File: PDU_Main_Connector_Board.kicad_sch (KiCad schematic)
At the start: 2 parts, among them J1 776228-1, J2 Conn_02x02_Odd_Even

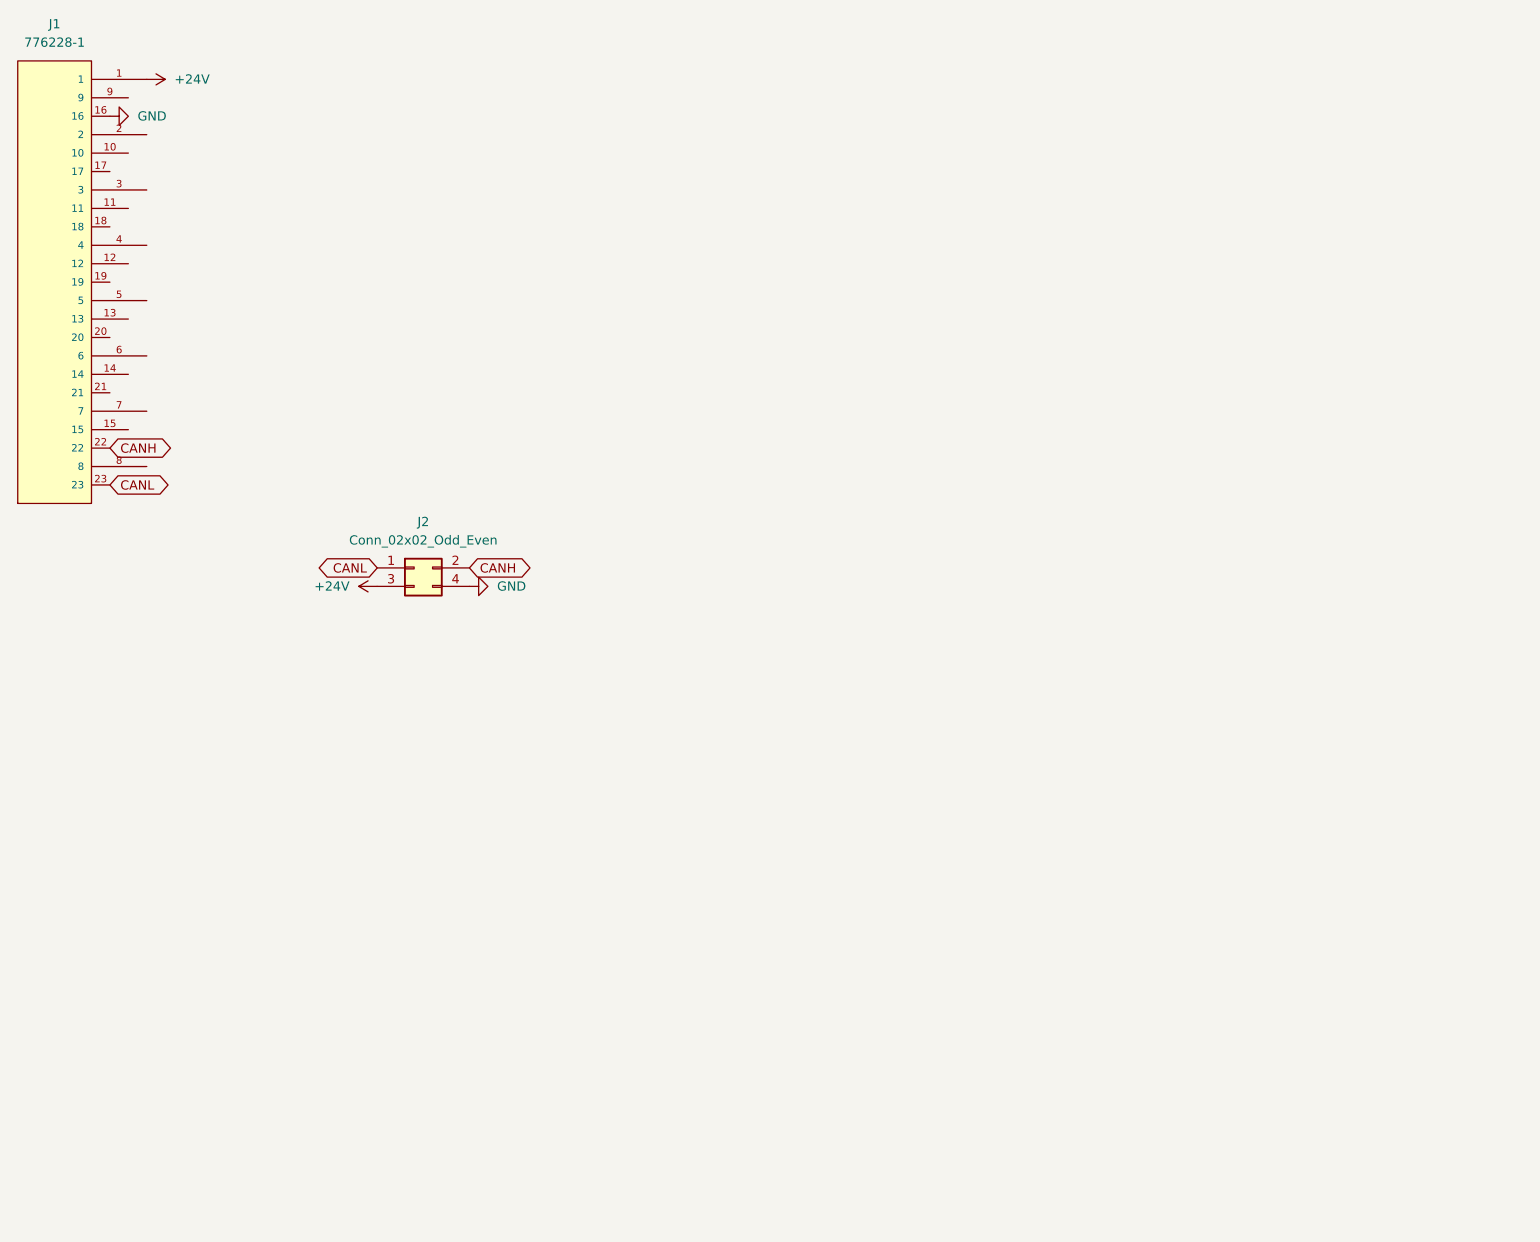
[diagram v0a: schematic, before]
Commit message: VER1.0: добавил схему по госту в доки, добавил дублирование CAN, добавил новые герберы
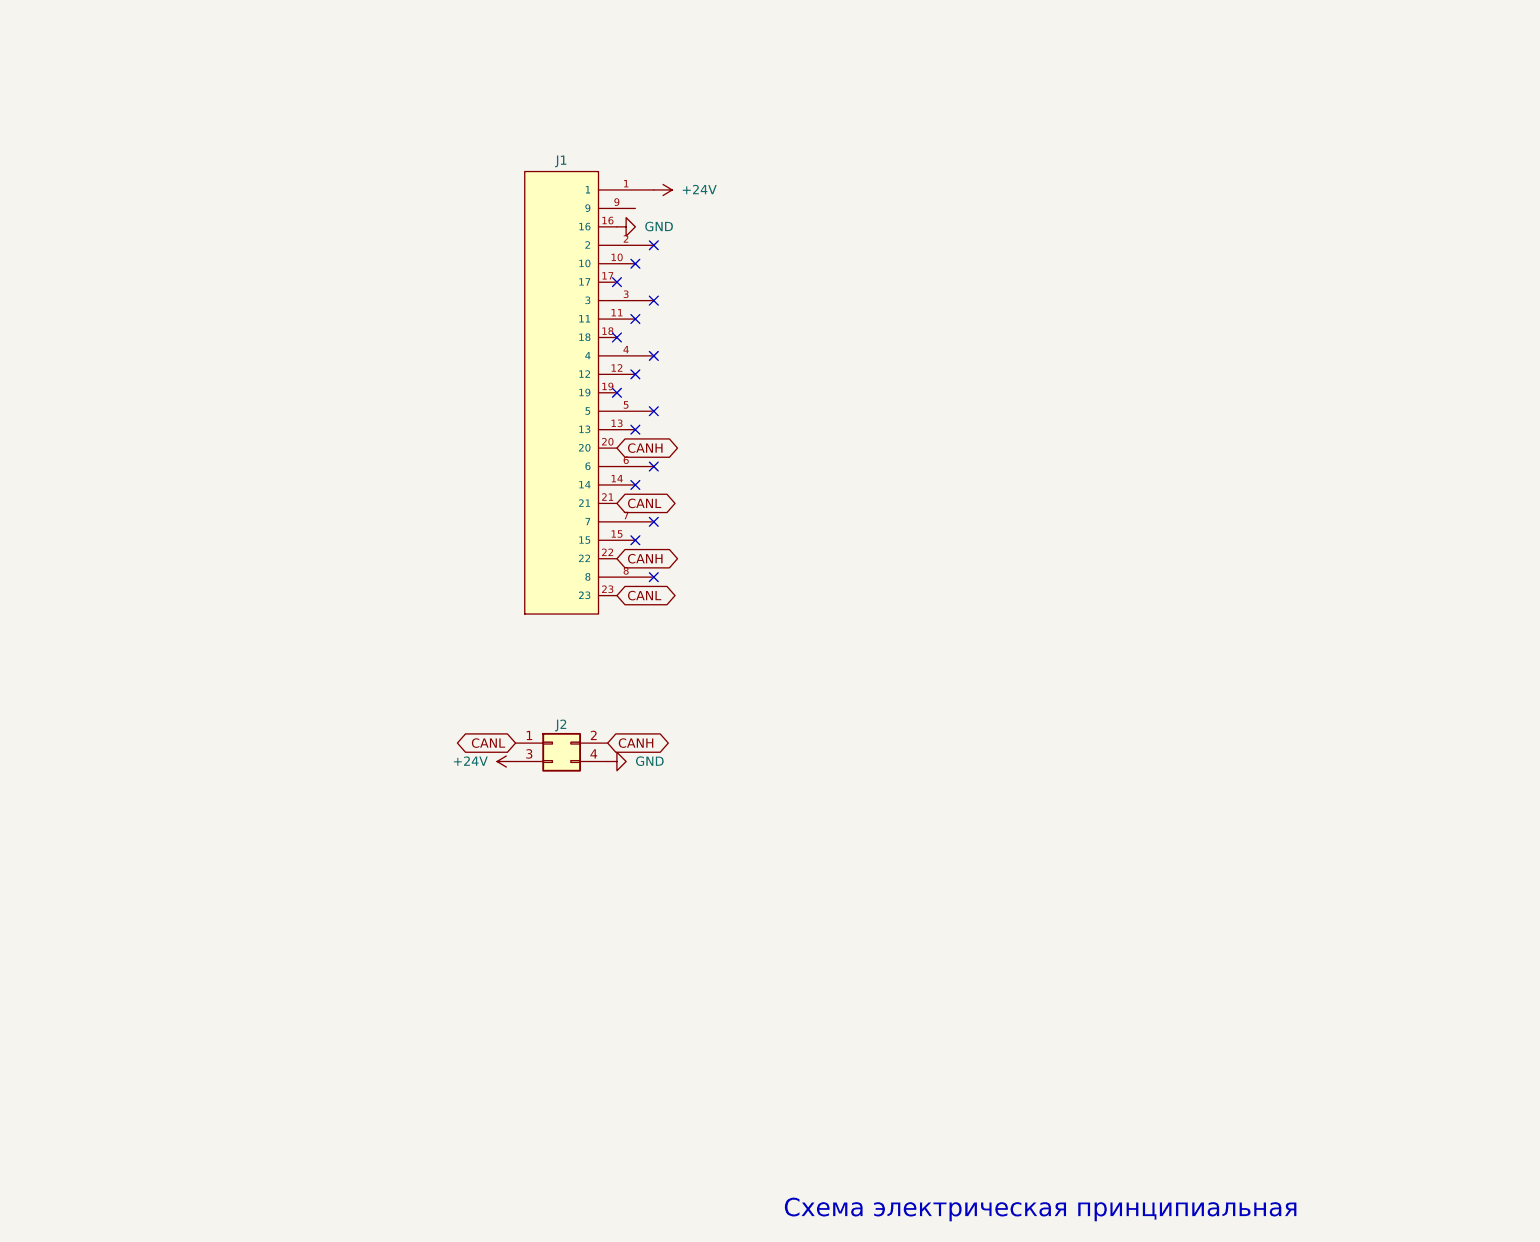
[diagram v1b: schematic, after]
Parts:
- J1: value 776228-1 -> ~; Availability In Stock -> (none); Check_prices https://www.snapeda.com/parts/776228-1/TE+Connectivity+AMP+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 -> (none); Comment 776228-1 -> (none); Description P/N (none) -> Connector; Description_1 AMPSEAL Series, 23 Way Through Hole Plug Power Conn, with S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 -> (none); MANUFACTURER TE CONNECTIVITY -> (none); MF TE Connectivity -> (none); MP 776228-1 -> (none); PARTREV C13 -> (none); Package None -> (none); Price None -> (none); Product Name (none) -> 301302311184; STANDARD MANUFACTURER RECOMMENDATIONS -> (none); SnapEDA_Link https://www.snapeda.com/parts/776228-1/TE+Connectivity+AMP+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 -> (none)
- J2: value Conn_02x02_Odd_Even -> ~; Description P/N (none) -> Connector; Product Name (none) -> DS1073-01-2x2MVT6
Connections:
- net CANH: now also J1.20
- net CANL: now also J1.21
- no-connect marks 0 -> 16
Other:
- note added: "Схема электрическая принципиальная"
- company: (none) -> ООО "Электротранспортные технологии"
- title: (none) -> Плата входного разъема
- moved on the sheet: J1, J2
